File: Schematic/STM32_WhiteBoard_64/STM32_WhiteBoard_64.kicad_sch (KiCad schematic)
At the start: 57 parts, among them J1 SWDIO+Serial, J2 USB_B_Micro, J3 Header1, J4 Header2, Q1 BC847BS, Q1 Si3493DDV, Q2 BC857BS, SW1 Boot0, SW2 Reset, U1 STM32F411RET6, U1 TPS54302, U2 W25Q32JVSSIQ, U3 TPS3828-33DBVR, X1 ASV-8MHz, Y1 ABS25-32.768KHZ-6-T

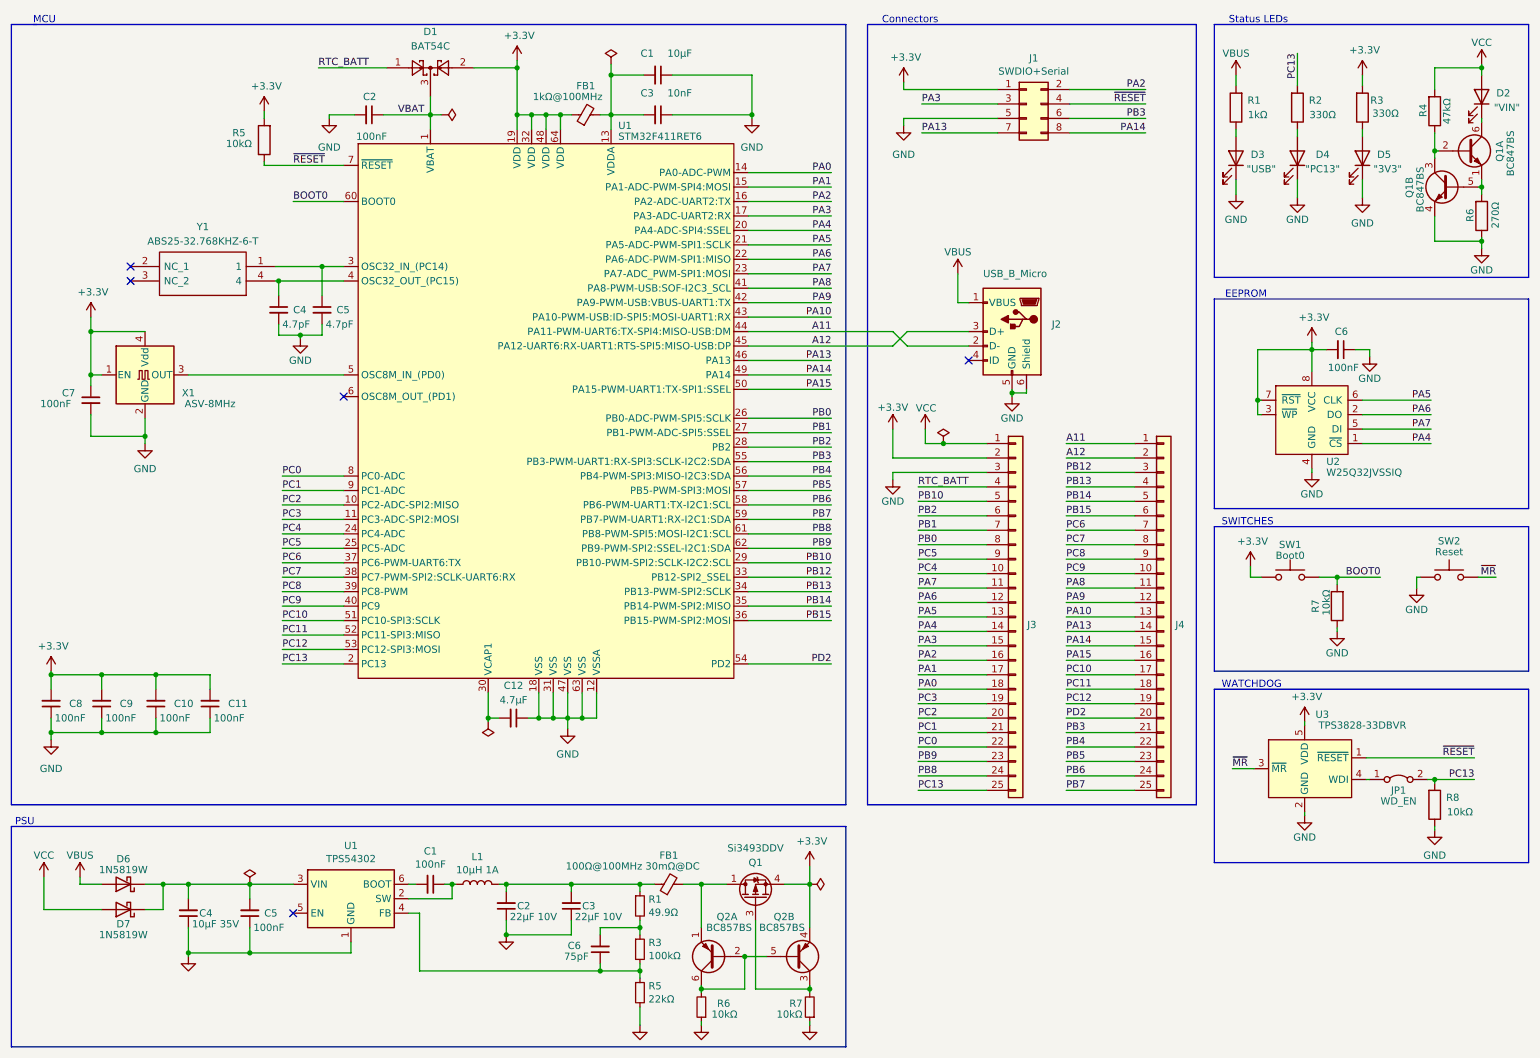
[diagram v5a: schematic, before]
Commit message: Added voltage reference
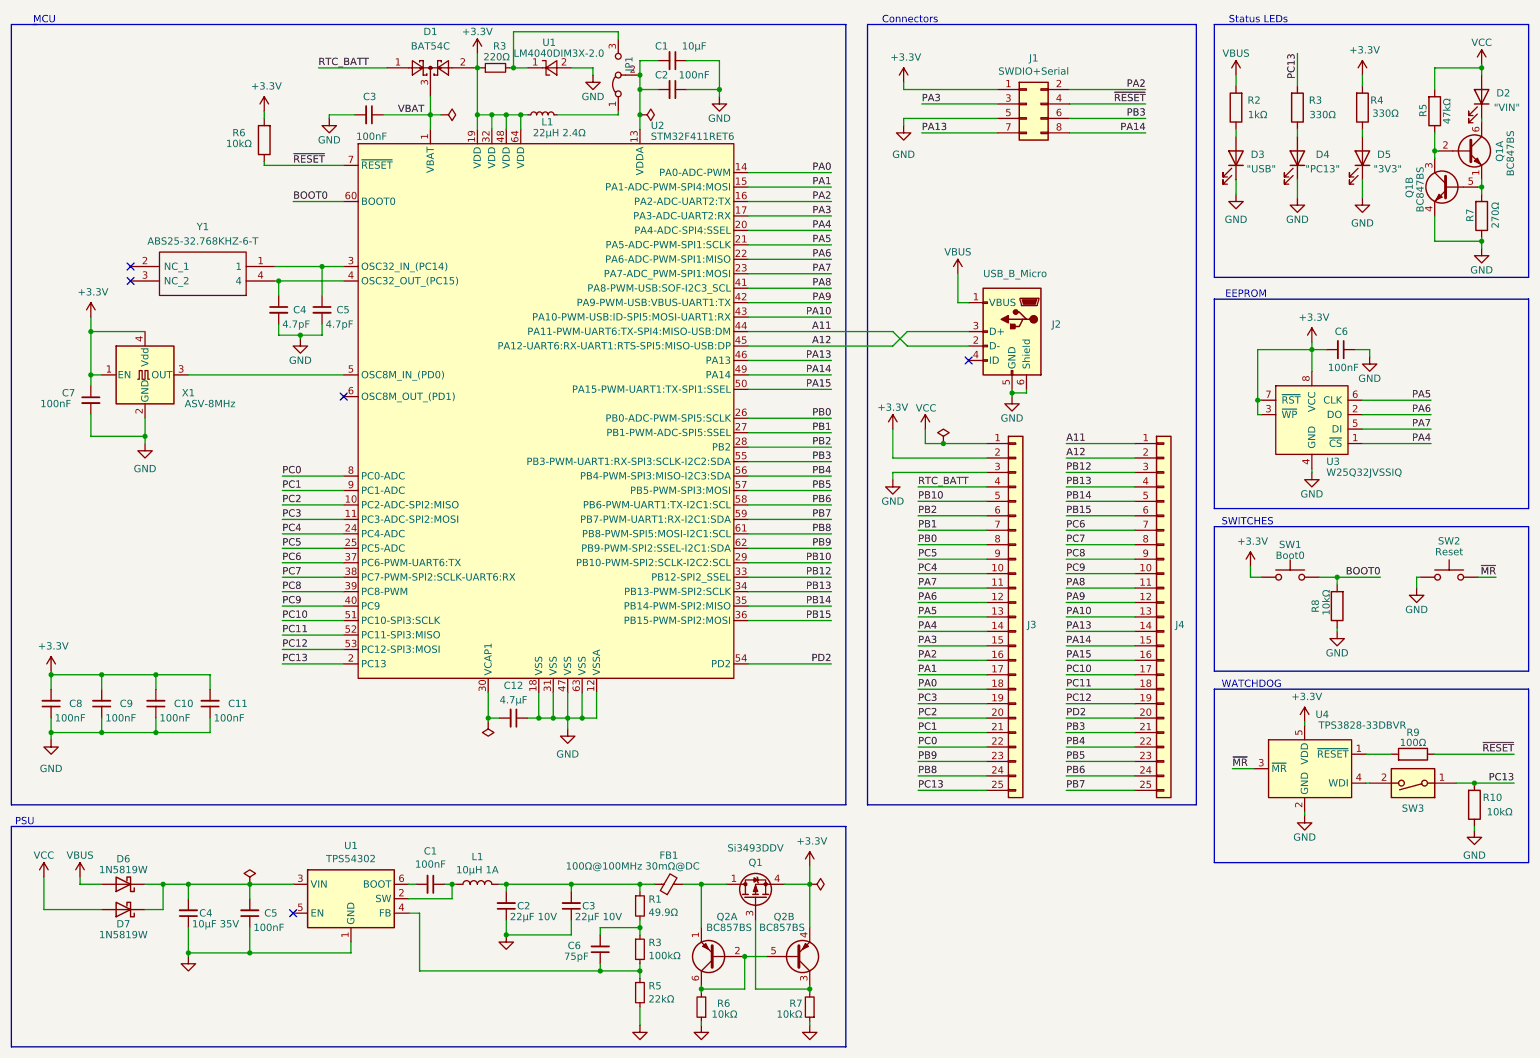
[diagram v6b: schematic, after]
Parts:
- removed JP1: WD_EN, myDevices:PinHeader_1x02_P1.27mm_Vertical, symbol Jumper:Jumper_2_Bridged
- added JP1: Jumper_3_Bridged12, Connector_PinHeader_1.27mm:PinHeader_1x03_P1.27mm_Vertical, symbol Jumper:Jumper_3_Bridged12
- added R3: 220Ω, Resistor_SMD:R_0603_1608Metric_Pad0.98x0.95mm_HandSolder, symbol Device:R_Small
- added R9: 100Ω, Resistor_SMD:R_0603_1608Metric_Pad0.98x0.95mm_HandSolder, symbol Device:R
- added SW3: SW_DIP_x01, Retronics_Switches:CFS0102TA, symbol Switch:SW_DIP_x01
- added U1: LM4040DIM3X-2.0, Package_TO_SOT_SMD:SOT-23, symbol Reference_Voltage:LM4040DBZ-2.0
- C2: renamed from C3; value 10nF -> 100nF
- L1: renamed from FB1; value 1kΩ@100MHz -> 22µH 2.4Ω; symbol Device:FerriteBead_Small -> Device:L_Small
- U3: renamed from U2; footprint Package_SO:SOIC-8_3.9x4.9mm_P1.27mm -> Retronics_Memory:W25Q32JVSSIQ
- renumbered C2 to C3, R8 to R10, R1 to R2, R2 to R3, R3 to R4, R4 to R5, R5 to R6, R6 to R7, R7 to R8, U1 to U2, U3 to U4
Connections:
- net +3.3V: now also R3.1
- net GND: now also U1.2 (A)
- net PC13: now also SW3.1
- net ~{RESET}: now also R9.1; no longer U4.1 (~{RESET})
- net at C1.2, C2.2, U2.13 (VDDA): now also JP1.2 (C); no longer L1.2
- net at U4.4 (WDI): now also SW3.2
- new net: JP1.3 (B), R3.2, U1.1 (K)
- new net: R9.2, U4.1 (~{RESET})
- new net: JP1.1 (A), L1.2
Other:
- moved on the sheet: C1, C2, R10

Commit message: Added btn PD2, added fuse, removed hardware watchdog
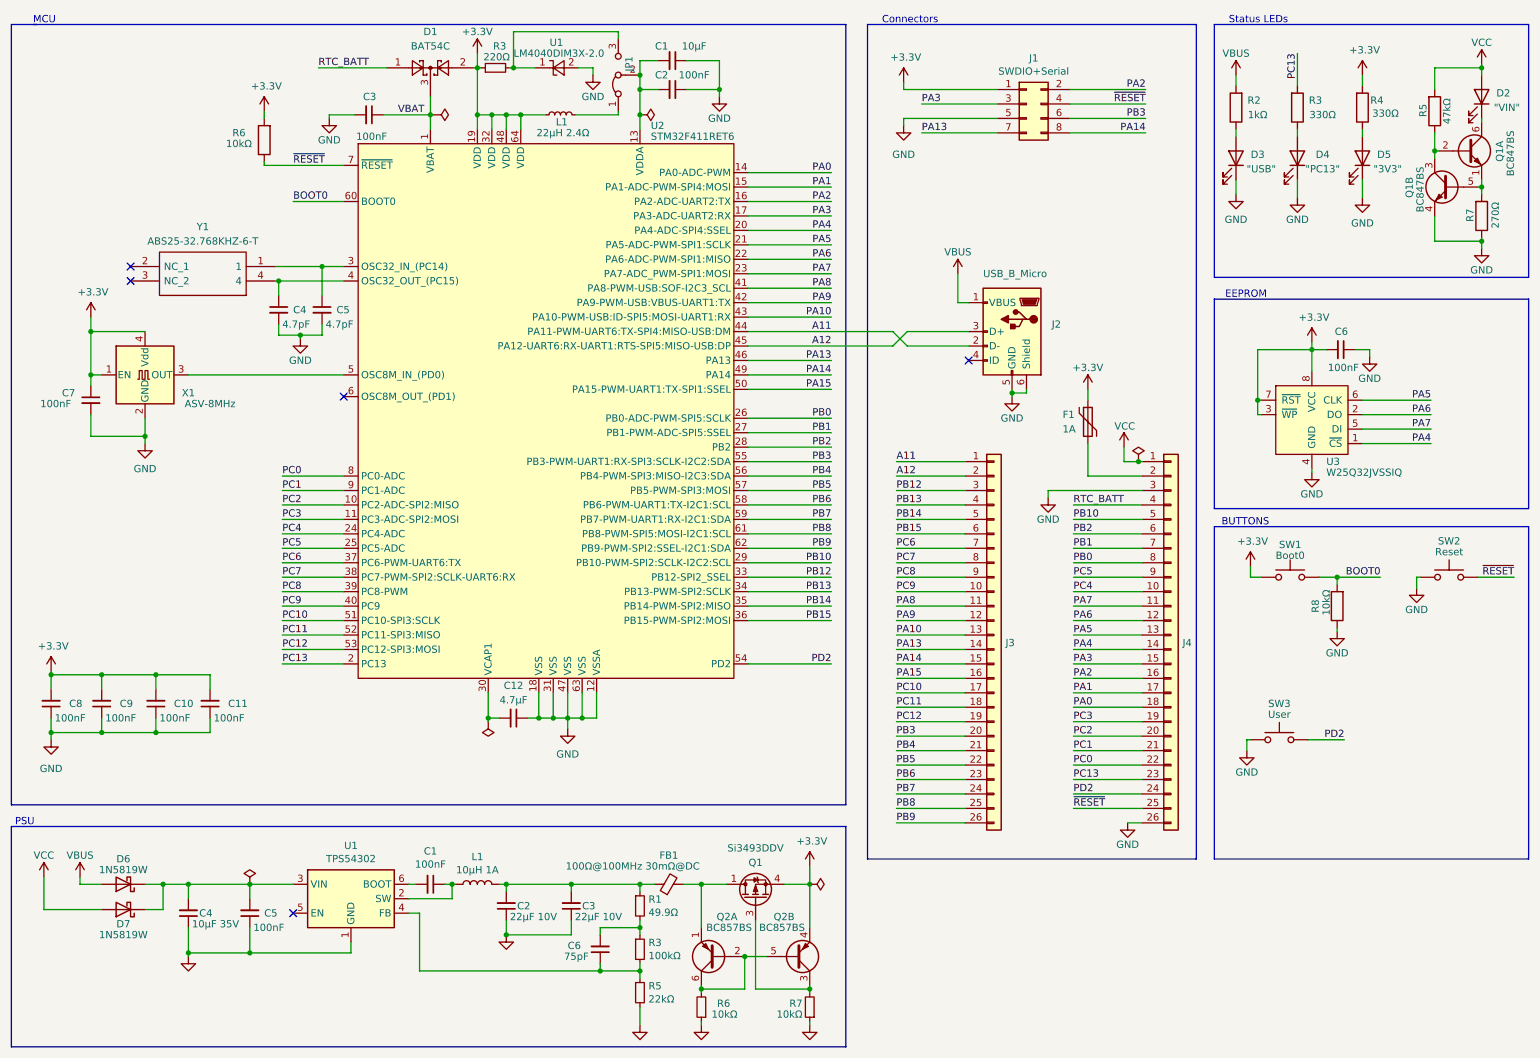
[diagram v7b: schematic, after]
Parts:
- removed R10: 10kΩ, Resistor_SMD:R_0603_1608Metric_Pad0.98x0.95mm_HandSolder, symbol Device:R
- removed R9: 100Ω, Resistor_SMD:R_0603_1608Metric_Pad0.98x0.95mm_HandSolder, symbol Device:R
- removed SW3: SW_DIP_x01, Retronics_Switches:CFS0102TA, symbol Switch:SW_DIP_x01
- removed U4: TPS3828-33DBVR, Package_TO_SOT_SMD:SOT-23-5_HandSoldering, symbol Retronics_Integrated_Circuits:TPS3828-33DBVR
- added F1: 1A, Fuse:Fuse_1206_3216Metric_Pad1.42x1.75mm_HandSolder, symbol Device:Polyfuse
- added SW3: User, myDevices:PTS840ESDGMSMTRLFS, symbol Switch:SW_Push
- J3: renamed from J4; footprint Connector_PinHeader_2.54mm:PinHeader_1x25_P2.54mm_Vertical -> Connector_PinHeader_2.54mm:PinHeader_1x26_P2.54mm_Vertical; symbol Connector_Generic:Conn_01x25 -> Connector_Generic:Conn_01x26
- J4: renamed from J3; footprint Connector_PinHeader_2.54mm:PinHeader_1x25_P2.54mm_Vertical -> Connector_PinHeader_2.54mm:PinHeader_1x26_P2.54mm_Vertical; symbol Connector_Generic:Conn_01x25 -> Connector_Generic:Conn_01x26
- Y1: footprint SamacSys_Parts:ABS25 -> SamacSys_Parts:ABS25-Retronics22
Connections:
- net ~{MR} is gone; now on net ~{RESET}: SW2.2
- net +3.3V: now also SW1.2, F1.1; no longer J4.2 (Pin_2), SW1.1
- net BOOT0: now also SW1.1; no longer SW1.2
- net GND: now also J4.26 (Pin_26), SW3.1
- net PB3: now also J3.20 (Pin_20); no longer J3.21 (Pin_21)
- net PB4: now also J3.21 (Pin_21); no longer J3.22 (Pin_22)
- net PB5: now also J3.22 (Pin_22); no longer J3.23 (Pin_23)
- net PB6: now also J3.23 (Pin_23); no longer J3.24 (Pin_24)
- net PB7: now also J3.24 (Pin_24); no longer J3.25 (Pin_25)
- net PB8: now also J3.25 (Pin_25); no longer J4.24 (Pin_24)
- net PB9: now also J3.26 (Pin_26); no longer J4.23 (Pin_23)
- net PC13: now also J4.23 (Pin_23); no longer J4.25 (Pin_25)
- net PD2: now also J4.24 (Pin_24), SW3.2; no longer J3.20 (Pin_20)
- net ~{RESET}: now also J4.25 (Pin_25)
- new net: F1.2, J4.2 (Pin_2)
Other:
- note added: "BUTTONS"
- note removed: "SWITCHES"
- note removed: "WATCHDOG"
- moved on the sheet: L1, U1

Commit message: Added basic code examples
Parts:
- C1: value 10µF -> 4.7µF
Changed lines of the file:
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@@
       (effects (font (size 1.27 1.27)))
     )
-    (property "Value" "10µF" (at 135.255 20.955 90)
+    (property "Value" "4.7µF" (at 135.255 20.955 90)
       (effects (font (size 1.27 1.27)))
     )
